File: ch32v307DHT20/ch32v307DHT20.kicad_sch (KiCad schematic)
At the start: 26 parts, among them SW1 SW_Push, U2 AMS1117-3.3, U3 RC1602A, U4 PCF8574, U5 3.3V to 5V, U6 DHT20, Y1 8MHz

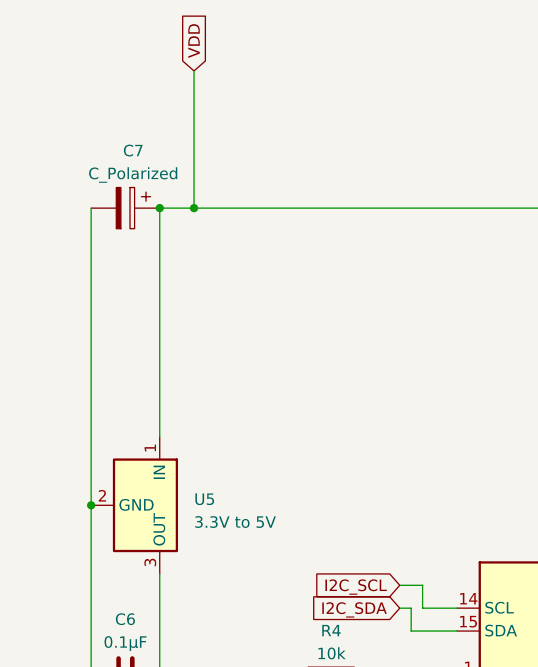
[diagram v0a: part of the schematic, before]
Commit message: add  condenser
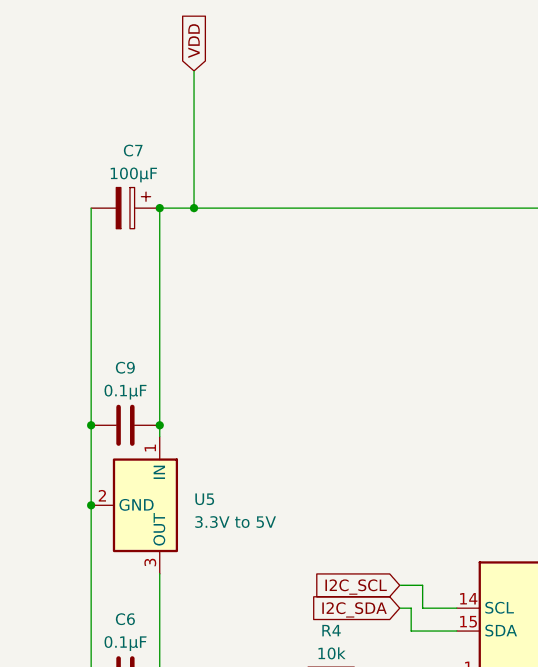
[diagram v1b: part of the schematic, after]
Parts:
- added C9: 0.1μF, symbol Device:C
- C7: value C_Polarized -> 100μF
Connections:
- net GNDREF: now also C9.1
- net VDD: now also C9.2
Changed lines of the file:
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@@
   (junction (at 25.4 55.88) (diameter 0) (color 0 0 0 0)
   )
+  (junction (at 36.83 138.43) (diameter 0) (color 0 0 0 0)
+  )
   (junction (at 243.84 121.92) (diameter 0) (color 0 0 0 0)
   )
@@
   )
   (junction (at 25.4 68.58) (diameter 0) (color 0 0 0 0)
+  )
+  (junction (at 29.21 138.43) (diameter 0) (color 0 0 0 0)
   )
   (junction (at 127 133.35) (diameter 0) (color 0 0 0 0)
@@
     (stroke (width 0) (type default))
   )
+  (wire (pts (xy 36.83 114.3) (xy 36.83 138.43))
+    (stroke (width 0) (type default))
+  )
   (wire (pts (xy 25.4 35.56) (xy 25.4 55.88))
     (stroke (width 0) (type default))
@@
     (stroke (width 0) (type default))
   )
+  (wire (pts (xy 29.21 114.3) (xy 29.21 138.43))
+    (stroke (width 0) (type default))
+  )
   (wire (pts (xy 154.94 146.05) (xy 154.94 153.67))
     (stroke (width 0) (type default))
@@
     (stroke (width 0) (type default))
   )
-  (wire (pts (xy 29.21 114.3) (xy 29.21 147.32))
-    (stroke (width 0) (type default))
-  )
   (wire (pts (xy 36.83 154.94) (xy 36.83 166.37))
     (stroke (width 0) (type default))
@@
     (stroke (width 0) (type default))
   )
-  (wire (pts (xy 36.83 114.3) (xy 36.83 139.7))
-    (stroke (width 0) (type default))
-  )
   (wire (pts (xy 63.5 168.91) (xy 63.5 186.69))
     (stroke (width 0) (type default))
@@
   )
   (wire (pts (xy 241.3 114.3) (xy 241.3 129.54))
+    (stroke (width 0) (type default))
+  )
+  (wire (pts (xy 36.83 138.43) (xy 36.83 139.7))
+    (stroke (width 0) (type default))
+  )
+  (wire (pts (xy 29.21 138.43) (xy 29.21 147.32))
     (stroke (width 0) (type default))
   )
@@
       (effects (font (size 1.27 1.27)))
     )
-    (property "Value" "C_Polarized" (at 33.909 110.49 90)
+    (property "Value" "100μF" (at 33.909 110.49 90)
       (effects (font (size 1.27 1.27)))
     )
@@
         )
       )
+    )
+  )
+  (symbol (lib_id "Device:C") (at 33.02 138.43 90) (unit 1)
+    (in_bom yes) (on_board yes) (dnp no) (fields_autoplaced)
+    (property "Reference" "C9" (at 33.02 132.08 90)
+      (effects (font (size 1.27 1.27)))
+    )
+    (property "Value" "0.1μF" (at 33.02 134.62 90)
+      (effects (font (size 1.27 1.27)))
+    )
+    (property "Footprint" "" (at 36.83 137.4648 0)
+      (effects (font (size 1.27 1.27)) hide)
+    )
+    (property "Datasheet" "~" (at 33.02 138.43 0)
+      (effects (font (size 1.27 1.27)) hide)
+    )
+    (pin "1")
+    (pin "2")
+    (instances
+      (project "ch32v307DHT20"
+        (path "/d3ff22a1-92a2-41ed-a90c-a40d37efb0f2"
+          (reference "C9") (unit 1)
+        )
+      )
